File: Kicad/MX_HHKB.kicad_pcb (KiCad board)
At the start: 2 copper layers, 285.8 x 95.2 mm, 158 parts, among them J1 USB_mini_micro_B, K1 K00, K10 K09, K11 K0A, K12 K0B, K13 K0C, K14 K10, K15 K11, K16 K12, K17 K13, K18 K14, K19 K15, K2 K01, K20 K16, K21 K17, K22 K18, K23 K19, K24 K1A, K25 K1B, K26 K1C, K27 K20, K28 K21, K29 K22, K3 K02, K30 K23, K31 K24, K32 K25, K33 K26, K34 K27, K35 K28, K36 K29, K37 K2A, K38 K2B, K39 K2C, K4 K03, K40 K30, K41 K31, K42 K32, K43 K33, K44 K34, K45 K35, K46 K36, K47 K37, K48 K38, K49 K39, K5 K04, K50 K3A, K51 K3B, K52 K3C, K53 K41, K54 K42, K55 K45, K56 K48, K57 K49, K58 K4A, K59 K4B, K6 K05, K60 K4C, K61 Ctrl, K62 L_ALT, K63 SPACE, K64 SPACE, K65 R_ALT, K66 R_ALT, K67 R_GUI, K68 R_GUI, K7 K06, K8 K07, K9 K08, SW1 SW_PUSH, U0 ATMEGA32U4, X1 XTAL_GND

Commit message: - Updated footprints - Fixed some bugs (position of holes)
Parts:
- added MXST: VAL**, Footprint:MXST, F.Cu at (342.9, 145.3)
- added MXST: VAL**, Footprint:MXST, F.Cu at (157.2, 183.4)
- added MXST: VAL**, Footprint:MXST, F.Cu at (257.2, 183.4)
- added MXST: VAL**, Footprint:MXST, F.Cu at (152.4, 183.4)
- added MXST: VAL**, Footprint:MXST, F.Cu at (266.7, 183.4)
- added MXST: VAL**, Footprint:MXST, F.Cu at (252.4, 183.4)
- added MXST: VAL**, Footprint:MXST, F.Cu at (319.1, 145.3)
- moved G*** 59.0 mm to (180.9, 181.5)
- moved D58 4.92 mm to (346.9, 118.6)
- moved G*** 3.78 mm to (235.2, 180.4)
- moved R5 2.95 mm to (74.4, 118.3)
- moved X1 2.04 mm to (97.6, 185.0)
- moved C8 1.94 mm to (89.3, 169.5)
- moved Poker_side_edge_long 1.46 mm to (351.7, 155.1)
- moved HOLE_M3 1.38 mm to (91.8, 126.6)
- moved Poker_side_edge_long 1.36 mm to (66.6, 155.1)
- moved Poker_oval_hole 1.23 mm to (326.9, 126.6)
- moved Poker_oval_hole 1.10 mm to (257.1, 183.8)
- moved Poker_oval_hole 0.93 mm to (194.8, 145.6)
- moved J1 0.83 mm to (85.8, 103.6)
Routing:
- net GND: track 291.1 -> 264.2 mm
- net /ESC_LED: track 77.1 -> 58.7 mm, vias 0 -> 2
- net /Row4: track 352.8 -> 363.8 mm
- net /Row1: track 472.6 -> 461.9 mm
- net /Col8: track 328.3 -> 320.2 mm
- net Net-(D58-Pad2): track 13.4 -> 19.6 mm
- net /Col9: track 386.1 -> 390.3 mm
- net /Col4: track 177.6 -> 181.8 mm
- net Net-(R4-Pad2): track 34.9 -> 30.8 mm
- net /Col12: track 357.8 -> 361.7 mm
- net /Col11: track 352.6 -> 356.3 mm
- net Net-(LD0-Pad2): track 4.27 -> 7.29 mm
- net Net-(C2-Pad1): track 11.6 -> 13.7 mm
- net Net-(R3-Pad1): track 30.2 -> 31.9 mm
- net VCC: track 147.9 -> 146.6 mm
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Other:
- board size 285.8 x 95.2 mm -> 285.1 x 95.6 mm
- board text added: "DK60 rev.A.1"
- board text removed: "DK60 rev.A"

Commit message: - Some updates in routing
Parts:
- moved D60 14.4 mm to (336.8, 116.8), turned to 270 degrees
- moved D52 13.7 mm to (328.0, 172.2), turned to 0 degrees
- moved D56 5.30 mm to (265.0, 181.0), turned to 0 degrees
- moved C3 3.93 mm to (71.8, 172.2)
- moved D39 3.00 mm to (339.8, 145.8)
- moved D32 2.45 mm to (192.5, 153.2)
- moved C7 2.25 mm to (71.8, 167.0)
- moved C6 2.25 mm to (77.8, 164.8)
- moved Poker_oval_hole 1.80 mm to (257.1, 185.6)
- moved C4 1.75 mm to (77.5, 159.8)
- moved C5 1.25 mm to (71.8, 162.2)
- moved J1 1.05 mm to (85.2, 104.5)
- moved Poker_oval_hole 0.91 mm to (326.8, 127.5)
- moved Poker_oval_hole 0.90 mm to (194.8, 146.5)
- moved Poker_side_edge_long 0.90 mm to (66.6, 156.0)
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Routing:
- net /Row0: track 604.5 -> 341.2 mm, vias 12 -> 2
- net /Row3: track 268.2 -> 255.5 mm
- net /Row1: track 461.9 -> 472.8 mm, vias 2 -> 4
- net /Col9: track 390.3 -> 380.3 mm
- net Net-(D52-Pad2): track 8.18 -> 15.3 mm
- net VCC: track 146.6 -> 151.3 mm
- net Net-(D60-Pad2): track 9.57 -> 5.14 mm
- net GND: track 264.2 -> 268.7 mm
- net Net-(D39-Pad2): track 12.0 -> 7.72 mm
- net Net-(J1-Pad2): track 67.8 -> 63.9 mm
- net Net-(J1-Pad3): track 72.5 -> 69.0 mm
- net Net-(D56-Pad2): track 33.7 -> 30.4 mm
- net /Col8: track 320.2 -> 317.5 mm
- net /Row4: track 363.8 -> 365.6 mm, vias 3 -> 5
- net /Col12: track 361.7 -> 360.5 mm
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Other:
- board size 285.1 x 95.6 mm -> 285.1 x 94.3 mm

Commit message: - Routing, again and again - Naming all Diodes - Fixed some bugs for holes - Added holes for PCB stabilizers
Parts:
- D1: value D -> D00
- D10: value D -> D09
- D11: value D -> D0A
- D12: value D -> D0B
- D13: value D -> D0C
- D14: value D -> D10
- D15: value D -> D11
- D16: value D -> D12
- D17: value D -> D13
- D18: value D -> D14
- D19: value D -> D15
- D2: value D -> D01
- D20: value D -> D16
- D21: value D -> D17
- D22: value D -> D18
- D23: value D -> D19
- D24: value D -> D1A
- D25: value D -> D1B
- D26: value D -> D1C
- D27: value D -> D20
- D28: value D -> D21
- D29: value D -> D22
- D3: value D -> D02
- D30: value D -> D23
- D31: value D -> D24
- D32: value D -> D25
- D33: value D -> D26
- D34: value D -> D27
- D35: value D -> D28
- D36: value D -> D29
- D37: value D -> D2A
- D38: value D -> D2B
- D39: value D -> D2C
- D4: value D -> D03
- D40: value D -> D30
- D41: value D -> D31
- D42: value D -> D32
- D43: value D -> D33
- D44: value D -> D34
- D45: value D -> D35
- D46: value D -> D36
- D47: value D -> D37
- D48: value D -> D38
- D49: value D -> D39
- D5: value D -> D04
- D50: value D -> D3A
- D51: value D -> D3B
- D52: value D -> D3C
- D53: value D -> D41
- D54: value D -> D42
- D55: value D -> D45
- D56: value D -> D48
- D57: value D -> D49
- D58: value D -> D4A
- D59: value D -> D4B
- D6: value D -> D05
- D60: value D -> D4C
- D7: value D -> D06
- D8: value D -> D07
- D9: value D -> D08
- moved D60 11.3 mm to (346.2, 123.0), turned to 180 degrees
- moved R2 9.15 mm to (70.8, 177.5), turned to 45 degrees
- moved D58 6.55 mm to (344.5, 112.5)
- moved R5 1.75 mm to (73.0, 117.2)
- moved C1 1.69 mm to (98.0, 179.0)
- moved C8 1.53 mm to (90.8, 169.4)
- moved R3 1.45 mm to (105.0, 157.2)
- moved R4 1.38 mm to (108.8, 161.0)
- moved D57 1.17 mm to (322.2, 181.4), turned to 180 degrees
- moved C4 0.46 mm to (77.8, 159.4), turned to 180 degrees
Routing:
- net /Row1: track 472.8 -> 589.5 mm, vias 4 -> 0
- net /Row3: track 255.5 -> 337.0 mm, vias 13 -> 7
- net GND: track 268.7 -> 323.2 mm, vias 0 -> 6
- net Net-(R1-Pad2): track 66.2 -> 83.2 mm, vias 2 -> 0
- net /Row0: track 341.2 -> 329.9 mm, vias 2 -> 4
- net VCC: track 151.3 -> 160.8 mm
- net Net-(D58-Pad2): track 19.6 -> 10.5 mm
- net /Col10: track 372.4 -> 368.1 mm
- net /Col11: track 356.5 -> 352.2 mm
- net Net-(R2-Pad1): track 9.86 -> 6.58 mm
- net /Col9: track 380.3 -> 377.5 mm, vias 2 -> 0
- net /Col1: track 118.4 -> 115.8 mm, vias 1 -> 2
- net Net-(R3-Pad1): track 31.9 -> 34.2 mm
- net /Col2: track 134.7 -> 132.9 mm
- net /Col12: track 360.5 -> 359.0 mm
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
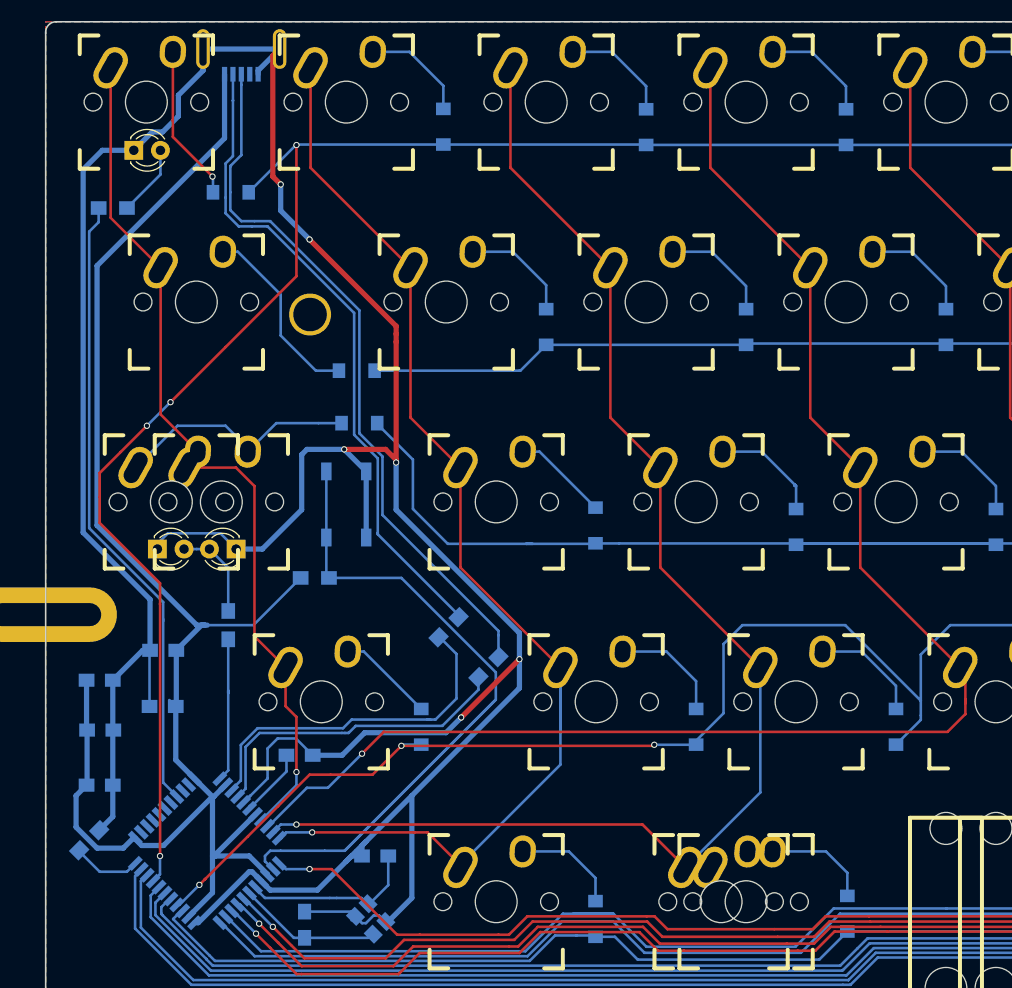
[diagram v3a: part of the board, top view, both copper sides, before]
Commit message: - Updated with of tracks for Vcc/Gnd
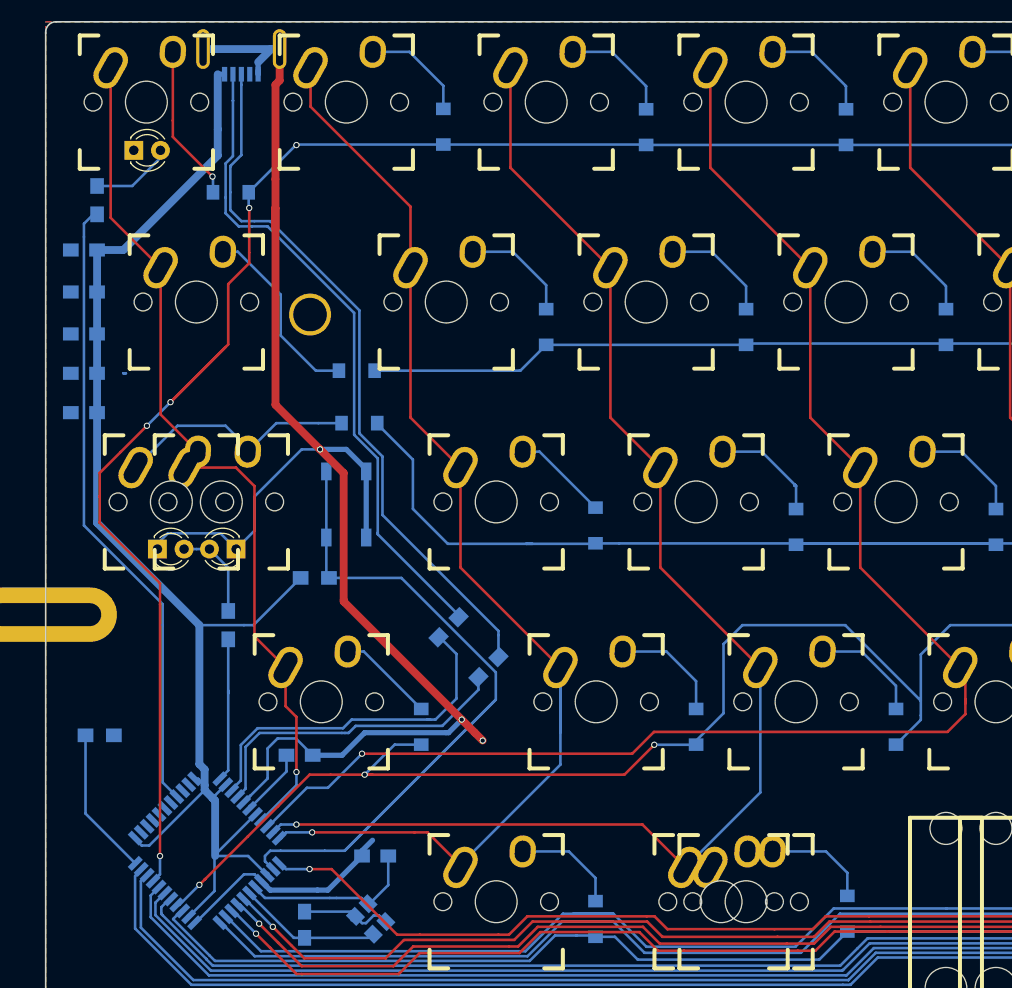
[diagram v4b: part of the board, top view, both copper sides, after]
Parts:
- moved C7 45.8 mm to (70.2, 121.2), turned to 180 degrees
- moved C6 40.2 mm to (70.2, 125.2)
- moved C3 35.5 mm to (70.2, 136.8), turned to 180 degrees
- moved C5 33.0 mm to (70.2, 129.2), turned to 180 degrees
- moved C4 27.5 mm to (70.2, 133.0)
- moved R2 10.0 mm to (71.8, 167.5), turned to 0 degrees
- moved R5 1.68 mm to (71.5, 116.5), turned to 90 degrees
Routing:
- net GND: track 323.2 -> 186.7 mm, vias 6 -> 3
- net VCC: track 160.8 -> 129.8 mm
- net Net-(R2-Pad1): track 6.58 -> 14.2 mm
- net /Row3: track 337.0 -> 342.2 mm
- net /Row0: track 329.9 -> 331.0 mm, vias 4 -> 5
- net Net-(LD0-Pad2): track 6.82 -> 7.86 mm
- net (no net): track 0.25 -> 0.75 mm

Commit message: - Updated plate.dxf (now use layers to simulate all available layouts) - Added revert 6u spacebar
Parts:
- added K69: K30, Footprint:Mx_Alps_225, F.Cu at (88.1, 164.3)
- added K70: K3C, Footprint:Mx_Alps_100, F.Cu at (342.9, 164.3)
- added K71: K3B, Footprint:Mx_Alps_175, F.Cu at (316.7, 164.3)
- added K72: SPACE, Footprint:Mx_Alps_100, F.Cu at (195.3, 183.4)
- added MXST: VAL**, Footprint:MXST, F.Cu at (100.0, 164.3)
- added MXST: VAL**, Footprint:MXST, F.Cu at (76.2, 164.3)
- moved G*** 99.2 mm to (334.2, 185.2)
- moved G*** 46.9 mm to (239.0, 184.5)
- moved G*** 6.10 mm to (176.5, 185.8)
- moved U0 4.43 mm to (80.6, 182.7)
- moved D51 4.29 mm to (319.5, 170.5)
- moved D52 3.75 mm to (324.2, 172.2)
- moved C1 2.67 mm to (98.8, 181.6)
- moved D32 2.47 mm to (190.8, 151.5), turned to 90 degrees
- moved D24 2.43 mm to (286.0, 131.0)
- moved D20 2.42 mm to (209.8, 131.0)
- moved D23 2.42 mm to (266.5, 131.0)
- moved D16 2.42 mm to (133.5, 131.0)
- moved D17 2.42 mm to (152.2, 131.0)
- moved D21 2.41 mm to (228.5, 131.0)
- moved D22 2.41 mm to (247.8, 131.0)
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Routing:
- net /Row1: track 589.5 -> 450.2 mm, vias 0 -> 2
- net GND: track 186.7 -> 115.9 mm
- net /Col9: track 377.5 -> 342.3 mm, vias 0 -> 2
- net /Row0: track 331.0 -> 308.7 mm, vias 5 -> 4
- net Net-(D55-Pad2): track 18.9 -> 40.2 mm
- net /Col12: track 359.0 -> 373.9 mm
- net Net-(R1-Pad2): track 83.2 -> 68.6 mm
- net Net-(D40-Pad2): track 9.27 -> 23.5 mm
- net /Col11: track 352.2 -> 366.0 mm
- net /Col0: track 86.1 -> 97.5 mm
- net /CAPS_LED: track 13.9 -> 24.3 mm
- net Net-(C8-Pad1): track 6.80 -> 17.1 mm
- net /Col5: track 241.9 -> 232.2 mm
- net Net-(D52-Pad2): track 15.3 -> 23.4 mm
- net /ESC_LED: track 59.9 -> 67.9 mm
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
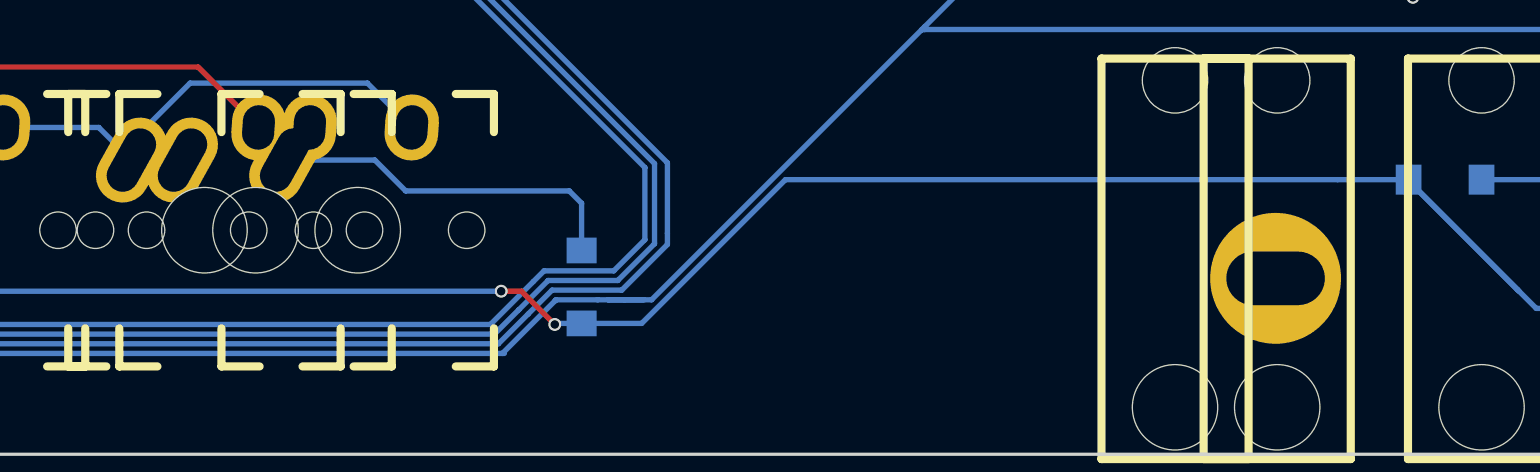
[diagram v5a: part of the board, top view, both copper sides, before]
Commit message: - Fixed bug for bottom hole in PCB - Generated Gerber files
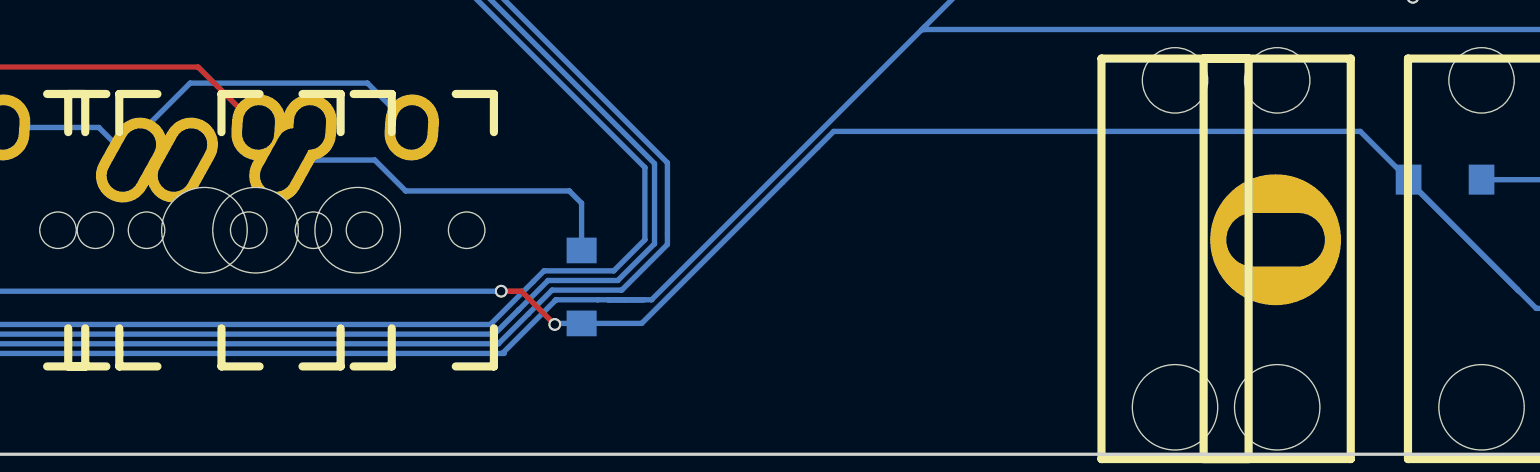
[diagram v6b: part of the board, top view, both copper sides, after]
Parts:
- moved Poker_oval_hole 1.80 mm to (257.1, 183.8)
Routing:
- net /Col5: track 232.2 -> 234.5 mm
- net /Row4: track 362.6 -> 364.4 mm
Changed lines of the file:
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@@
   (general
     (links 255)
-    (no_connects 1)
-    (area 66.524999 99.424999 351.775001 193.875001)
+    (no_connects 0)
+    (area 33.750002 85.500001 374.65 202.9)
     (thickness 1.6)
-    (drawings 25)
-    (tracks 1108)
+    (drawings 26)
+    (tracks 1111)
     (zones 0)
     (modules 171)
@@
     (47 F.CrtYd user)
     (48 B.Fab user)
-    (49 F.Fab user hide)
+    (49 F.Fab user)
   )
   (setup
@@
   )
   (module Footprint:Poker_oval_hole (layer F.Cu)
-    (at 257.1 185.6)
+    (at 257.1 183.8)
     (fp_text reference Poker_oval_hole (at 0 0) (layer F.SilkS) hide
       (effects (font (size 1 1) (thickness 0.15)))
@@
       (net 79 /Col5))
   )
+  (gr_line (start 257.1 183.8) (end 257.1 184.3) (angle 90) (layer Cmts.User) (width 0.2))
+  (gr_line (start 66.6 185.6) (end 66.3 185.6) (angle 90) (layer Cmts.User) (width 0.2))
   (gr_line (start 202.40625 176.2125) (end 188.11875 190.5) (angle 90) (layer Cmts.User) (width 0.2))
-  (gr_line (start 202.40625 190.5) (end 202.40625 176.2125) (angle 90) (layer Cmts.User) (width 0.2))
   (gr_line (start 188.11875 176.2125) (end 202.40625 190.5) (angle 90) (layer Cmts.User) (width 0.2))
   (dimension 24.9 (width 0.3) (layer Dwgs.User)
@@
   (segment (start 116.46625 178.56625) (end 119 181.1) (width 0.25) (layer B.Cu) (net 62))
   (segment (start 116.46625 178.56625) (end 112.0575 178.56625) (width 0.25) (layer B.Cu) (net 62))
+  (segment (start 235.75 179.5) (end 236.5 178.75) (width 0.25) (layer B.Cu) (net 63))
+  (segment (start 261.05 178.75) (end 263.3 181) (width 0.25) (layer B.Cu) (net 63) (status 800000))
+  (segment (start 236.5 178.75) (end 261.05 178.75) (width 0.25) (layer B.Cu) (net 63))
+  (segment (start 234.125 181.125) (end 235.75 179.5) (width 0.25) (layer B.Cu) (net 63))
   (segment (start 332.875 148.625) (end 332.761398 148.625) (width 0.25) (layer B.Cu) (net 63))
   (segment (start 341.125 148.625) (end 347.9 141.85) (width 0.25) (layer B.Cu) (net 63))
@@
   (segment (start 323.9 157.486398) (end 323.9 181.4) (width 0.25) (layer B.Cu) (net 63))
   (segment (start 332.761398 148.625) (end 323.9 157.486398) (width 0.25) (layer B.Cu) (net 63))
-  (segment (start 260 181) (end 234.25 181) (width 0.25) (layer B.Cu) (net 63))
-  (segment (start 234.25 181) (end 227.55 187.7) (width 0.25) (layer B.Cu) (net 63))
+  (segment (start 234.125 181.125) (end 227.55 187.7) (width 0.25) (layer B.Cu) (net 63))
   (segment (start 263.3 181) (end 263.3 181.05) (width 0.25) (layer B.Cu) (net 63))
   (segment (start 263.3 181.05) (end 269.25 187) (width 0.25) (layer B.Cu) (net 63))
@@
   (segment (start 110.825 190.9) (end 115.15 186.575) (width 0.25) (layer B.Cu) (net 63))
   (segment (start 224.75 187.7) (end 227.55 187.7) (width 0.25) (layer B.Cu) (net 63))
-  (segment (start 260 181) (end 263.3 181) (width 0.25) (layer B.Cu) (net 63))
   (segment (start 221 186.2) (end 221.95 186.2) (width 0.25) (layer F.Cu) (net 63))
   (segment (start 223.55 187.7) (end 224.75 187.7) (width 0.25) (layer B.Cu) (net 63))
@@
   (segment (start 158.52 122.93625) (end 158.52 137.22375) (width 0.25) (layer F.Cu) (net 78))
   (segment (start 158.52 137.22375) (end 163.2825 141.98625) (width 0.25) (layer F.Cu) (net 78))
+  (segment (start 203.76375 180.08625) (end 206.145 180.08625) (width 0.25) (layer B.Cu) (net 79))
   (segment (start 203.76375 180.08625) (end 203.76375 179.23625) (width 0.25) (layer B.Cu) (net 79))
   (segment (start 203.76375 179.23625) (end 206.5 176.5) (width 0.25) (layer B.Cu) (net 79))
